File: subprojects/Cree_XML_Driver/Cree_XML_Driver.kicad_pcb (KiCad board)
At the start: 2 copper layers, 20.2 x 17.5 mm, 58 parts, among them J101 PJ-102AH, J102 Conn_01x03, Q101 Si2302CDS-T1, Q102 Si2302CDS-T1, Q103 Si2302CDS-T1, Q104 Si2302CDS-T1, U101 PAM2804, U102 PAM2804, U103 PAM2804, U104 PAM2804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

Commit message: Led horiz
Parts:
- LOGO101: moved to B.Cu
- TP101: footprint TestPoint:TestPoint_THTPad_2.0x2.0mm_Drill1.0mm -> TestPoint:TestPoint_THTPad_D1.0mm_Drill0.5mm
- U105, U107: footprint Package_SO:SO-8_3.9x4.9mm_P1.27mm -> Package_SO:SOIC-8_3.9x4.9mm_P1.27mm
- moved MK102 104.0 mm to (163.8, 94.0)
- moved MK103 86.2 mm to (163.8, 120.7)
- moved MK101 76.8 mm to (95.2, 94.0)
- moved TP101 62.2 mm to (150.7, 111.6), turned to 90 degrees
- moved R113 61.5 mm to (146.9, 120.2), turned to 90 degrees
- moved R117 60.7 mm to (151.0, 120.4), turned to 270 degrees
- moved C111 58.9 mm to (148.4, 106.1)
- moved C110 57.7 mm to (148.4, 92.7), turned to 180 degrees
- moved R118 56.9 mm to (146.9, 106.1), turned to 270 degrees
- moved R122 55.8 mm to (150.0, 114.4), turned to 270 degrees
- moved J102 55.7 mm to (164.7, 113.5), turned to 180 degrees
- moved U107 54.8 mm to (145.4, 110.4), turned to 0 degrees
- moved MK104 50.2 mm to (95.2, 120.7)
- moved C109 50.0 mm to (148.4, 120.2)
- moved D102 48.1 mm to (162.2, 112.2), turned to 270 degrees
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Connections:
- U105 pad 7: Net-(U105-Pad7) -> (no net)
- U107 pad 7: Net-(U107-Pad7) -> (no net)
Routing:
- net +5V: track 184.4 -> 94.4 mm
- net /PWM_R: track 57.0 -> 8.05 mm
- net Net-(C109-Pad1): track 46.7 -> 1.54 mm
- net /PWM_BB: track 50.9 -> 6.52 mm, vias 2 -> 1
- net /PWM_G: track 44.9 -> 8.82 mm, vias 6 -> 2
- net Net-(R117-Pad1): track 38.9 -> 7.27 mm, vias 0 -> 1
- net Net-(R119-Pad1): track 46.5 -> 15.9 mm, vias 4 -> 2
- net GND: track 287.5 -> 315.7 mm, vias 9 -> 35
- net /DIN: track 26.1 -> 0.00 mm, vias 2 -> 0
- net Net-(R114-Pad1): track 55.0 -> 31.2 mm
- net Net-(R120-Pad1): track 46.4 -> 23.3 mm, vias 3 -> 2
- net /PWM_B: track 32.5 -> 14.6 mm
- net Net-(R121-Pad1): track 46.0 -> 28.5 mm
- net Net-(R115-Pad1): track 43.5 -> 28.8 mm
- net /PWM_BW: track 20.0 -> 5.31 mm, vias 2 -> 0
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- added copper zone on B.Cu, net GND
- added copper zone on F.Cu, net Net-(L101-Pad1)
- added copper zone on F.Cu, net Net-(L102-Pad1)
- added copper zone on F.Cu, net Net-(L103-Pad1)
- added copper zone on F.Cu, net Net-(L104-Pad1)
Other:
- board size 20.2 x 17.5 mm -> 76.2 x 34.3 mm

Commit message: Finish up led
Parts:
- added JP101: SolderJumper_3_Bridged12, Jumper:SolderJumper-3_P1.3mm_Bridged12_Pad1.0x1.5mm, B.Cu at (95.3, 100.7)
- added JP102: SolderJumper_3_Bridged12, Jumper:SolderJumper-3_P1.3mm_Bridged12_Pad1.0x1.5mm, B.Cu at (95.3, 103.2)
- added JP103: SolderJumper_3_Bridged12, Jumper:SolderJumper-3_P1.3mm_Bridged12_Pad1.0x1.5mm, B.Cu at (95.3, 105.7)
- added JP104: SolderJumper_3_Bridged12, Jumper:SolderJumper-3_P1.3mm_Bridged12_Pad1.0x1.5mm, B.Cu at (95.3, 108.2)
- J102: footprint Connector_PinSocket_1.27mm:PinSocket_1x03_P1.27mm_Vertical -> Connector_PinHeader_2.54mm:PinHeader_1x03_P2.54mm_Horizontal
- TP101: footprint TestPoint:TestPoint_THTPad_D1.0mm_Drill0.5mm -> TestPoint:TestPoint_THTPad_1.0x1.0mm_Drill0.5mm
- moved LOGO101 55.6 mm to (157.2, 121.3)
- moved J102 8.65 mm to (157.2, 109.2), turned to 0 degrees
- moved D102 8.39 mm to (154.2, 109.6)
- moved R117 3.81 mm to (150.8, 116.6), turned to 0 degrees
- moved J101 1.84 mm to (153.6, 102.3)
- moved R111 1.40 mm to (95.7, 113.5)
- moved R122 1.14 mm to (150.7, 113.5), turned to 180 degrees
- moved R112 1.07 mm to (95.6, 109.0), turned to 180 degrees
- moved MK101 0.64 mm to (95.2, 93.3)
- moved MK102 0.64 mm to (163.8, 93.3)
- moved MK103 0.63 mm to (163.8, 121.3)
- moved MK104 0.63 mm to (95.2, 121.3)
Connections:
- R109 pad 2: /PWM_BB -> /PWM_BG
- R110 pad 2: /PWM_BB -> /PWM_BR
- U106 pad 10: /PWM_BB -> Net-(JP101-Pad1)
- U106 pad 12: /PWM_BW -> Net-(JP101-Pad3)
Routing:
- net Net-(JP101-Pad1): track 0.00 -> 103.7 mm, vias 0 -> 3
- net Net-(JP101-Pad3): track 0.00 -> 101.2 mm, vias 0 -> 3
- net +5V: track 94.4 -> 109.2 mm
- net Net-(C109-Pad1): track 1.54 -> 10.6 mm, vias 0 -> 2
- net /DIN: track 0.00 -> 8.12 mm, vias 0 -> 1
- net Net-(R122-Pad1): track 0.00 -> 7.16 mm
- net Net-(R122-Pad2): track 0.00 -> 6.93 mm, vias 0 -> 2
- net Net-(R117-Pad1): track 7.27 -> 2.25 mm, vias 1 -> 0
- net Net-(D102-Pad2): track 0.00 -> 3.75 mm
- net /PWM_BR: track 0.00 -> 3.01 mm, vias 0 -> 1
- net /PWM_BB: track 6.52 -> 3.61 mm
- net Net-(Q104-Pad1): track 0.00 -> 1.53 mm
- net Net-(Q101-Pad1): track 0.00 -> 1.41 mm
- net /PWM_BG: track 0.00 -> 1.37 mm, vias 0 -> 1
- net /PWM_W: track 25.5 -> 26.9 mm
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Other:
- board size 76.2 x 34.3 mm -> 76.2 x 35.6 mm
- board text added: "1A RGBW Driver r0, 10/29/20"
- board text added: "5V"
- board text added: "B"
- board text added: "DIN"
- board text added: "G"
- board text added: "GND"
- board text added: "Notch: face up"
- board text added: "R"
- board text added: "T"
- board text added: "W"

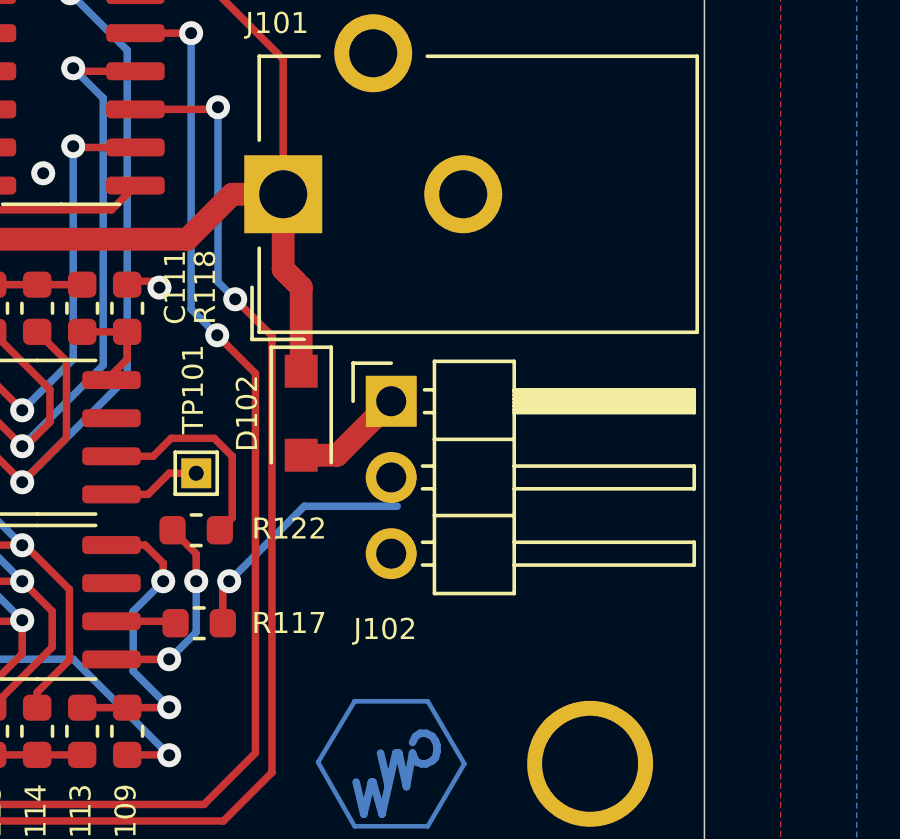
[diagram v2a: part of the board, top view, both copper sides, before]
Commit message: Add JST cable for easier integration
Carries power, data and ground over a JST 1.25mm
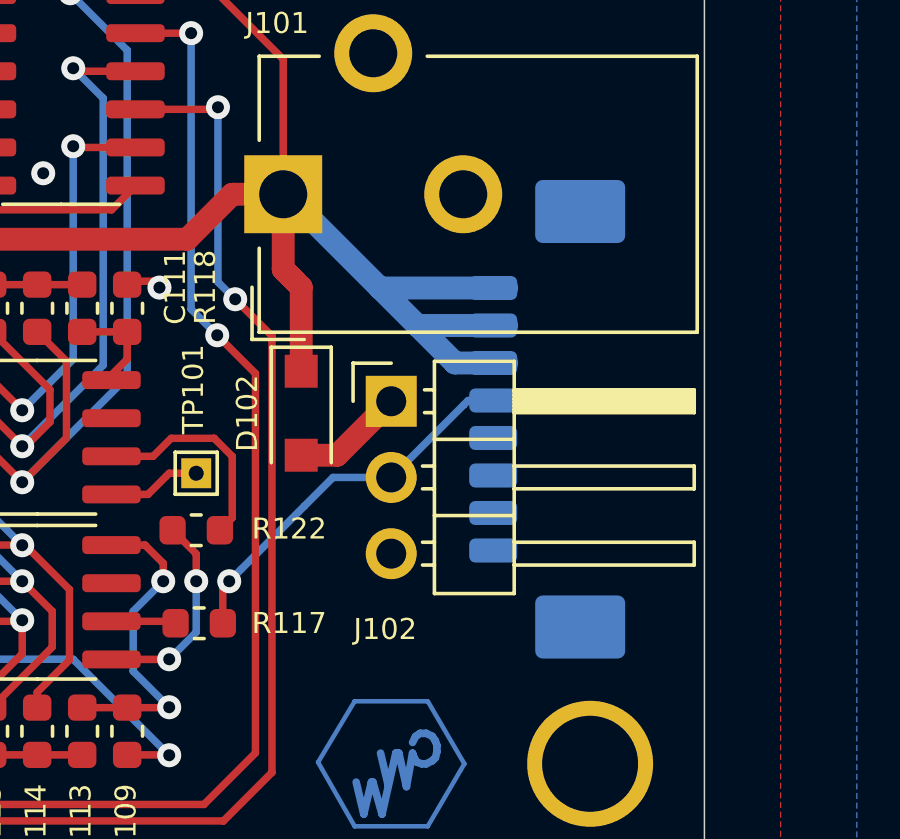
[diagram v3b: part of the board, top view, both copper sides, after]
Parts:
- added J103: JST 1.25mm, Connector_Molex:Molex_PicoBlade_53261-0871_1x08-1MP_P1.25mm_Horizontal, B.Cu at (163.0, 109.8)
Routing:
- net +5V: track 109.2 -> 126.1 mm
- net /DIN: track 8.12 -> 13.2 mm
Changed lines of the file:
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@@
   (general
     (thickness 1.6)
-    (drawings 17)
-    (tracks 552)
+    (drawings 18)
+    (tracks 562)
     (zones 0)
-    (modules 62)
+    (modules 63)
     (nets 47)
   )
@@
       (net 44 "Net-(JP101-Pad3)"))
   )
-  (gr_text 5V (at 166.9 109.13904) (layer B.SilkS)
+  (module Connector_Molex:Molex_PicoBlade_53261-0871_1x08-1MP_P1.25mm_Horizontal (layer B.Cu)
+    (at 163 109.8 270)
+    (descr "Molex PicoBlade series connector, 53261-0871 (http://www.molex.com/pdm_docs/sd/532610271_sd.pdf), generated with kicad-footprint-generator")
+    (tags "connector Molex PicoBlade top entry")
+    (attr smd)
+    (fp_text reference J103 (at 0 4.4 90) (layer B.SilkS)
+      (effects (font (size 1 1) (thickness 0.15)) (justify mirror))
+    )
+    (fp_text value "JST 1.25mm" (at 0 -3.8 90) (layer B.Fab)
+      (effects (font (size 1 1) (thickness 0.15)) (justify mirror))
+    )
+    (fp_line (start -4.375 0.892893) (end -3.875 1.6) (layer B.Fab) (width 0.1))
+    (fp_line (start -4.875 1.6) (end -4.375 0.892893) (layer B.Fab) (width 0.1))
+    (fp_line (start 8.48 3.7) (end -8.48 3.7) (layer B.CrtYd) (width 0.05))
+    (fp_line (start 8.48 -3.1) (end 8.48 3.7) (layer B.CrtYd) (width 0.05))
+    (fp_line (start -8.48 -3.1) (end 8.48 -3.1) (layer B.CrtYd) (width 0.05))
+    (fp_line (start -8.48 3.7) (end -8.48 -3.1) (layer B.CrtYd) (width 0.05))
+    (fp_line (start 7.375 -2.2) (end 5.875 -2.2) (layer B.Fab) (width 0.1))
+    (fp_line (start 7.375 -1.6) (end 7.375 -2.2) (layer B.Fab) (width 0.1))
+    (fp_line (start 7.575 -1.4) (end 7.375 -1.6) (layer B.Fab) (width 0.1))
+    (fp_line (start 7.575 0.4) (end 7.575 -1.4) (layer B.Fab) (width 0.1))
+    (fp_line (start 7.375 0.6) (end 7.575 0.4) (layer B.Fab) (width 0.1))
+    (fp_line (start 5.875 0.6) (end 7.375 0.6) (layer B.Fab) (width 0.1))
+    (fp_line (start -7.375 -2.2) (end -5.875 -2.2) (layer B.Fab) (width 0.1))
+    (fp_line (start -7.375 -1.6) (end -7.375 -2.2) (layer B.Fab) (width 0.1))
+    (fp_line (start -7.575 -1.4) (end -7.375 -1.6) (layer B.Fab) (width 0.1))
+    (fp_line (start -7.575 0.4) (end -7.575 -1.4) (layer B.Fab) (width 0.1))
+    (fp_line (start -7.375 0.6) (end -7.575 0.4) (layer B.Fab) (width 0.1))
+    (fp_line (start -5.875 0.6) (end -7.375 0.6) (layer B.Fab) (width 0.1))
+    (fp_line (start 5.875 1.6) (end 5.875 -2.6) (layer B.Fab) (width 0.1))
+    (fp_line (start -5.875 1.6) (end -5.875 -2.6) (layer B.Fab) (width 0.1))
+    (fp_line (start -5.875 -2.6) (end 5.875 -2.6) (layer B.Fab) (width 0.1))
+    (fp_line (start 5.985 -2.71) (end 5.985 -2.26) (layer B.SilkS) (width 0.12))
+    (fp_line (start -5.985 -2.71) (end 5.985 -2.71) (layer B.SilkS) (width 0.12))
+    (fp_line (start -5.985 -2.26) (end -5.985 -2.71) (layer B.SilkS) (width 0.12))
+    (fp_line (start 5.985 1.71) (end 5.035 1.71) (layer B.SilkS) (width 0.12))
+    (fp_line (start 5.985 1.26) (end 5.985 1.71) (layer B.SilkS) (width 0.12))
+    (fp_line (start -5.035 1.71) (end -5.035 3.2) (layer B.SilkS) (width 0.12))
+    (fp_line (start -5.985 1.71) (end -5.035 1.71) (layer B.SilkS) (width 0.12))
+    (fp_line (start -5.985 1.26) (end -5.985 1.71) (layer B.SilkS) (width 0.12))
+    (fp_line (start -5.875 1.6) (end 5.875 1.6) (layer B.Fab) (width 0.1))
+    (fp_text user %R (at 0 -1.9 90) (layer B.Fab)
+      (effects (font (size 1 1) (thickness 0.15)) (justify mirror))
+    )
+    (pad 1 smd roundrect (at -4.375 2.4 270) (size 0.8 1.6) (layers B.Cu B.Paste B.Mask) (roundrect_rratio 0.25)
+      (net 1 +5V))
+    (pad 2 smd roundrect (at -3.125 2.4 270) (size 0.8 1.6) (layers B.Cu B.Paste B.Mask) (roundrect_rratio 0.25)
+      (net 1 +5V))
+    (pad 3 smd roundrect (at -1.875 2.4 270) (size 0.8 1.6) (layers B.Cu B.Paste B.Mask) (roundrect_rratio 0.25)
+      (net 1 +5V))
+    (pad 4 smd roundrect (at -0.625 2.4 270) (size 0.8 1.6) (layers B.Cu B.Paste B.Mask) (roundrect_rratio 0.25)
+      (net 14 /DIN))
+    (pad 5 smd roundrect (at 0.625 2.4 270) (size 0.8 1.6) (layers B.Cu B.Paste B.Mask) (roundrect_rratio 0.25)
+      (net 2 GND))
+    (pad 6 smd roundrect (at 1.875 2.4 270) (size 0.8 1.6) (layers B.Cu B.Paste B.Mask) (roundrect_rratio 0.25)
+      (net 2 GND))
+    (pad 7 smd roundrect (at 3.125 2.4 270) (size 0.8 1.6) (layers B.Cu B.Paste B.Mask) (roundrect_rratio 0.25)
+      (net 2 GND))
+    (pad 8 smd roundrect (at 4.375 2.4 270) (size 0.8 1.6) (layers B.Cu B.Paste B.Mask) (roundrect_rratio 0.25)
+      (net 2 GND))
+    (pad MP smd roundrect (at -6.925 -0.5 270) (size 2.1 3) (layers B.Cu B.Paste B.Mask) (roundrect_rratio 0.119048)
+      (net 2 GND))
+    (pad MP smd roundrect (at 6.925 -0.5 270) (size 2.1 3) (layers B.Cu B.Paste B.Mask) (roundrect_rratio 0.119048)
+      (net 2 GND))
+    (model ${KISYS3DMOD}/Connector_Molex.3dshapes/Molex_PicoBlade_53261-0871_1x08-1MP_P1.25mm_Horizontal.wrl
+      (at (xyz 0 0 0))
+      (scale (xyz 1 1 1))
+      (rotate (xyz 0 0 0))
+    )
+  )
+  (gr_text 5V (at 159.1 105.4) (layer B.SilkS)
+    (effects (font (size 0.762 0.762) (thickness 0.1524)) (justify left mirror))
+  )
+  (gr_text 5V (at 165.4 109.23904) (layer B.SilkS)
     (effects (font (size 0.762 0.762) (thickness 0.1524)) (justify left mirror))
   )
-  (gr_text GND (at 166.9 114.21904) (layer B.SilkS)
+  (gr_text GND (at 165.4 114.31904) (layer B.SilkS)
     (effects (font (size 0.762 0.762) (thickness 0.1524)) (justify left mirror))
   )
-  (gr_text DIN (at 166.9 111.67904) (layer B.SilkS)
+  (gr_text DIN (at 165.4 111.77904) (layer B.SilkS)
     (effects (font (size 0.762 0.762) (thickness 0.1524)) (justify left mirror))
   )
@@
   (segment (start 139.8 119.8) (end 139.8 120.8) (width 0.762) (layer F.Cu) (net 1))
   (segment (start 139.8 120.8) (end 139.8 121.6) (width 0.762) (layer F.Cu) (net 1))
+  (segment (start 161.05 105.425) (end 156.825 105.425) (width 0.762) (layer B.Cu) (net 1))
+  (segment (start 156.825 105.425) (end 153.7 102.3) (width 0.762) (layer B.Cu) (net 1))
+  (segment (start 158.075 106.675) (end 156.825 105.425) (width 0.762) (layer B.Cu) (net 1))
+  (segment (start 161.05 106.675) (end 158.075 106.675) (width 0.762) (layer B.Cu) (net 1))
+  (segment (start 159.325 107.925) (end 158.075 106.675) (width 0.762) (layer B.Cu) (net 1))
+  (segment (start 161.05 107.925) (end 159.325 107.925) (width 0.762) (layer B.Cu) (net 1))
   (via (at 100.3 116.6) (size 0.8) (drill 0.4) (layers F.Cu B.Cu) (net 2))
   (via (at 99.2 116.6) (size 0.8) (drill 0.4) (layers F.Cu B.Cu) (net 2))
@@
   (segment (start 151.5875 116.6) (end 151.5875 115.4125) (width 0.25) (layer F.Cu) (net 14))
   (via (at 151.8 115.2) (size 0.8) (drill 0.4) (layers F.Cu B.Cu) (net 14))
-  (segment (start 157.4 112.7) (end 154.3 112.7) (width 0.25) (layer B.Cu) (net 14))
   (segment (start 152.199999 114.800001) (end 151.8 115.2) (width 0.25) (layer B.Cu) (net 14))
   (segment (start 151.5875 115.4125) (end 151.8 115.2) (width 0.25) (layer F.Cu) (net 14))
   (segment (start 154.3 112.7) (end 152.199999 114.800001) (width 0.25) (layer B.Cu) (net 14))
+  (segment (start 155.26 111.74) (end 154.3 112.7) (width 0.25) (layer B.Cu) (net 14))
+  (segment (start 157.2 111.74) (end 155.26 111.74) (width 0.25) (layer B.Cu) (net 14))
+  (segment (start 159.765 109.175) (end 159.62 109.32) (width 0.25) (layer B.Cu) (net 14))
+  (segment (start 161.05 109.175) (end 159.765 109.175) (width 0.25) (layer B.Cu) (net 14))
+  (segment (start 157.2 111.74) (end 159.62 109.32) (width 0.25) (layer B.Cu) (net 14))
   (segment (start 100.2 102.2) (end 101.5 102.2) (width 0.762) (layer F.Cu) (net 15))
   (segment (start 100 103.1) (end 100 102.4) (width 0.762) (layer F.Cu) (net 15))

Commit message: BOM update and text cleanup
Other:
- board text added: "D"

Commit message: Prep for gerber export
Update fields
Align standoff holes
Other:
- rule pad_to_mask_clearance: 0.05 -> 0
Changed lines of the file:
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@@
     (pad_size 1.524 1.524)
     (pad_drill 0.762)
-    (pad_to_mask_clearance 0.05)
+    (pad_to_mask_clearance 0)
     (aux_axis_origin 0 0)
     (visible_elements 7FFFFFFF)
@@
       (layerselection 0x010fc_ffffffff)
       (usegerberextensions false)
-      (usegerberattributes true)
+      (usegerberattributes false)
       (usegerberadvancedattributes true)
       (creategerberjobfile true)
@@
       (psa4output false)
       (plotreference true)
-      (plotvalue true)
+      (plotvalue false)
       (plotinvisibletext false)
       (padsonsilk false)
@@
       (outputformat 1)
       (mirror false)
-      (drillshape 1)
+      (drillshape 0)
       (scaleselection 1)
-      (outputdirectory ""))
+      (outputdirectory "gerber/"))
   )
   (net 0 "")
@@
     (pad 8 smd roundrect (at 4.375 2.4 270) (size 0.8 1.6) (layers B.Cu B.Paste B.Mask) (roundrect_rratio 0.25)
       (net 2 GND))
-    (pad MP smd roundrect (at -6.925 -0.5 270) (size 2.1 3) (layers B.Cu B.Paste B.Mask) (roundrect_rratio 0.119048)
-      (net 2 GND))
-    (pad MP smd roundrect (at 6.925 -0.5 270) (size 2.1 3) (layers B.Cu B.Paste B.Mask) (roundrect_rratio 0.119048)
+    (pad MP smd roundrect (at -6.925 -0.5 270) (size 2.1 3) (layers B.Cu B.Paste B.Mask) (roundrect_rratio 0.119047619047619)
+      (net 2 GND))
+    (pad MP smd roundrect (at 6.925 -0.5 270) (size 2.1 3) (layers B.Cu B.Paste B.Mask) (roundrect_rratio 0.119047619047619)
       (net 2 GND))
     (model ${KISYS3DMOD}/Connector_Molex.3dshapes/Molex_PicoBlade_53261-0871_1x08-1MP_P1.25mm_Horizontal.wrl

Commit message: Soldermask clearance fix
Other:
- rule pad_to_mask_clearance: 0 -> 0.0508
